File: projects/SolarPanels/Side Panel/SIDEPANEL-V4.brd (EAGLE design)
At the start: 99.5 x 82.5 mm, 27 parts

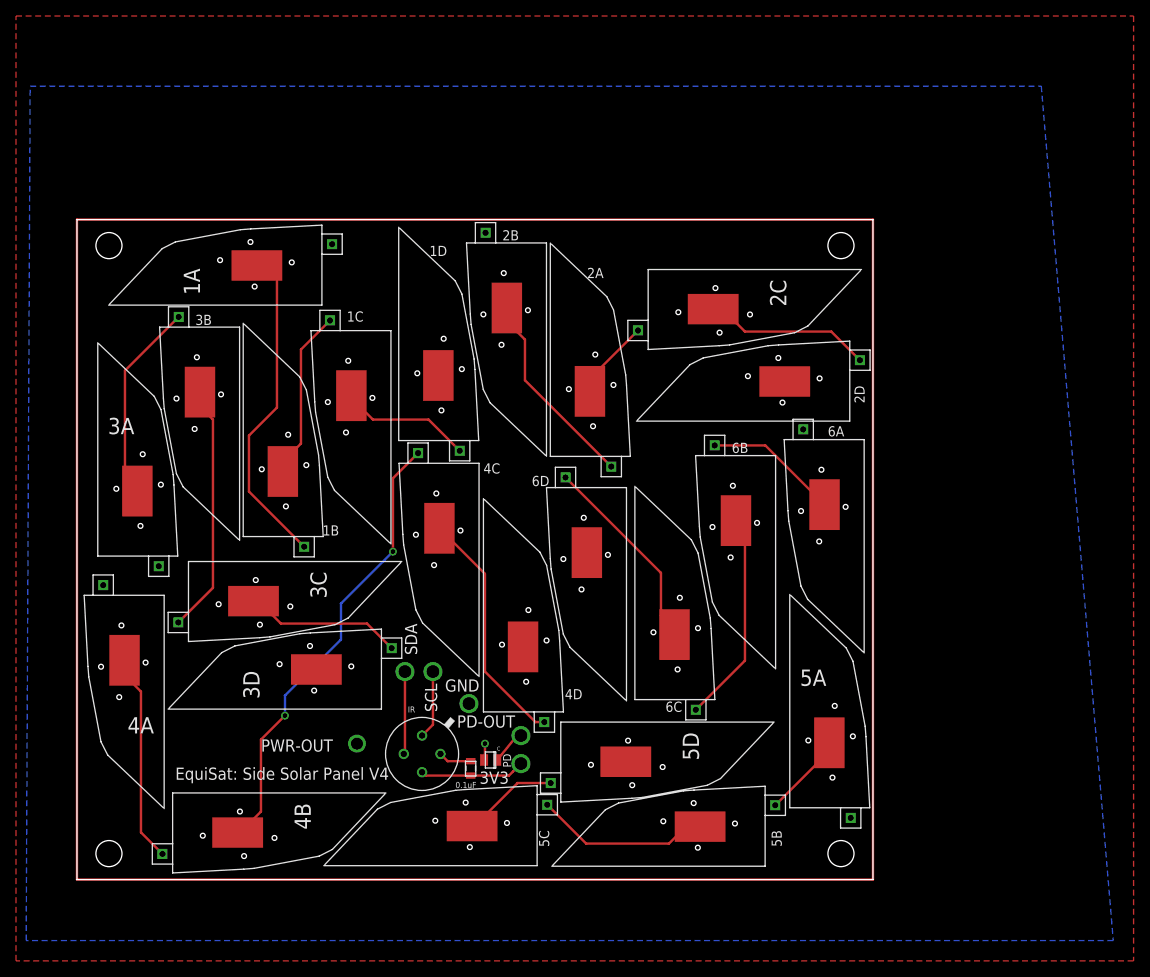
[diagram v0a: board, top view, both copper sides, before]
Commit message: Added top panel v4
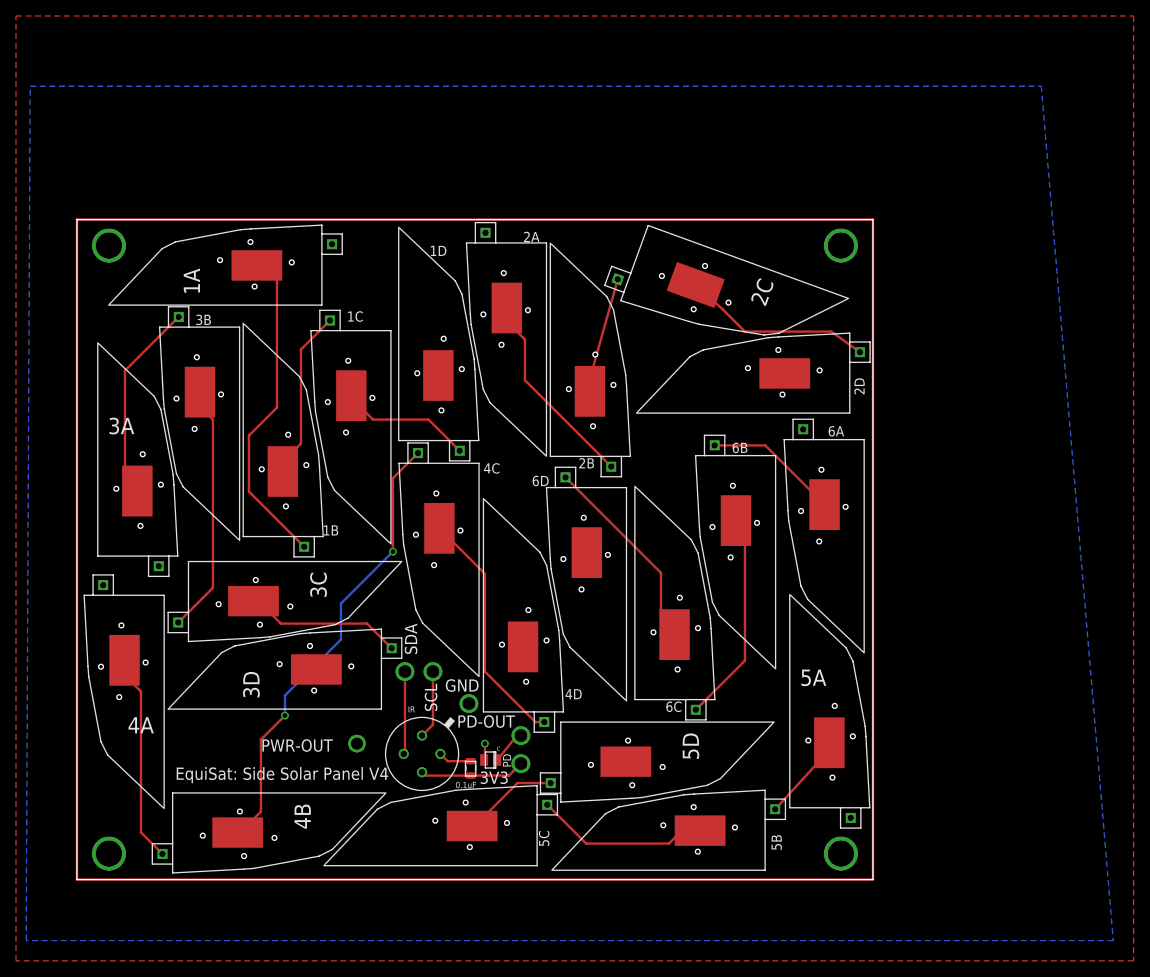
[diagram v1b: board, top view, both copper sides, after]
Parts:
- moved 2C 5.50 mm to (71.4, 81.8), turned to 250 degrees
- moved 2D 1.00 mm to (96.6, 58.3)
- moved 5B 0.50 mm to (86.0, 1.17)
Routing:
- net 2C: track 10.1 -> 14.5 mm
- net N$2: track 21.0 -> 23.7 mm
- net GND: vias 2 -> 6
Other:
- board text added: "September 2016"
- board text removed: "August 2016"
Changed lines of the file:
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@@
 <setting verticaltext="up"/>
 </settings>
-<grid distance="19.6850394" unitdist="mil" unit="mil" style="lines" multiple="1" display="no" altdistance="1.96850394" altunitdist="mil" altunit="mil"/>
+<grid distance="0.5" unitdist="mm" unit="mm" style="lines" multiple="1" display="no" altdistance="0.05" altunitdist="mm" altunit="mm"/>
 <layers>
 <layer number="1" name="Top" color="4" fill="1" visible="yes" active="yes"/>
@@
 <wire x1="99.5" y1="82.5" x2="0" y2="82.5" width="0" layer="20"/>
 <wire x1="0" y1="82.5" x2="0" y2="0" width="0" layer="20"/>
-<hole x="4" y="3.25" drill="3.26"/>
-<hole x="4" y="79.25" drill="3.26"/>
-<hole x="95.5" y="3.25" drill="3.26"/>
-<hole x="95.5" y="79.25" drill="3.26"/>
 <text x="32.5" y="16.5" size="1.524" layer="22" rot="MR0">PWR-OUT</text>
 <text x="40.5" y="24.5" size="1.524" layer="22" rot="MR270">SDA</text>
@@
 <text x="50.5" y="24" size="1.524" layer="22" rot="MR0">GND</text>
 <text x="38" y="50.5" size="1.524" layer="22" rot="MR270">EquiSat: Side Solar Panel V4</text>
-<text x="35.5" y="42" size="1.524" layer="22" rot="MR270">August 2016</text>
+<text x="35.5" y="42" size="1.524" layer="22" rot="MR270">September 2016</text>
 <text x="39" y="14" size="1.524" layer="21" rot="R180">EquiSat: Side Solar Panel V4</text>
 <text x="23" y="16" size="1.524" layer="21">PWR-OUT</text>
@@
 <polygon width="0.4064" layer="30">
 <vertex x="0" y="0"/>
-<vertex x="9" y="0"/>
-<vertex x="9" y="18"/>
-<vertex x="18" y="18"/>
-<vertex x="18" y="24"/>
-<vertex x="9" y="24"/>
-<vertex x="9" y="83.5"/>
+<vertex x="6.5" y="0"/>
+<vertex x="6.5" y="83.5"/>
 <vertex x="-5" y="83.5"/>
 <vertex x="-5" y="0"/>
@@
 </polygon>
 <polygon width="0.4064" layer="30">
-<vertex x="99.5" y="0"/>
-<vertex x="90.5" y="0"/>
-<vertex x="90.5" y="17.5"/>
-<vertex x="81" y="17.5"/>
-<vertex x="81" y="23.5"/>
-<vertex x="90.5" y="23.5"/>
-<vertex x="90.5" y="84.5"/>
+<vertex x="106.5" y="0"/>
+<vertex x="92" y="0"/>
+<vertex x="92" y="17.5"/>
+<vertex x="92.5" y="17.5"/>
+<vertex x="92.5" y="84.5"/>
 <vertex x="106.5" y="84.5"/>
-<vertex x="106.5" y="0"/>
 </polygon>
 </plain>
@@
 </element>
 <element name="1A" library="Solar Panel Parts" package="SOLARCELL2" value="NEWSOLARPANEL" x="30.62" y="71.81" rot="R90"/>
-<element name="2D" library="Solar Panel Parts" package="SOLARCELL2" value="NEWSOLARPANEL" x="96.6" y="57.31" smashed="yes" rot="R90">
-<attribute name="NAME" x="81.36" y="58.58" size="2.032" layer="25" rot="R90"/>
-<attribute name="NAME" x="97.19" y="61.75" size="1.27" layer="21" rot="R270"/>
-</element>
-<element name="2C" library="Solar Panel Parts" package="SOLARCELL2" value="NEWSOLARPANEL" x="71.4" y="76.26" rot="R270"/>
+<element name="2D" library="Solar Panel Parts" package="SOLARCELL2" value="NEWSOLARPANEL" x="96.6" y="58.31" smashed="yes" rot="R90">
+<attribute name="NAME" x="81.36" y="59.58" size="2.032" layer="25" rot="R90"/>
+<attribute name="NAME" x="97.19" y="62.75" size="1.27" layer="21" rot="R270"/>
+</element>
+<element name="2C" library="Solar Panel Parts" package="SOLARCELL2" value="NEWSOLARPANEL" x="71.4" y="81.76" rot="R250"/>
 <element name="2B" library="Solar Panel Parts" package="SOLARCELL2" value="NEWSOLARPANEL" x="59.17" y="52.9" smashed="yes">
 <attribute name="NAME" x="60.44" y="68.14" size="2.032" layer="25"/>
-<attribute name="NAME" x="55.25" y="81.17" size="1.27" layer="21" rot="R180"/>
+<attribute name="NAME" x="64.75" y="52.67" size="1.27" layer="21" rot="R180"/>
 </element>
 <element name="2A" library="Solar Panel Parts" package="SOLARCELL2" value="NEWSOLARPANEL" x="58.69" y="79.58" smashed="yes" rot="R180">
 <attribute name="NAME" x="57.42" y="64.34" size="2.032" layer="25" rot="R180"/>
-<attribute name="NAME" x="63.77" y="75.19" size="1.27" layer="21"/>
+<attribute name="NAME" x="55.77" y="79.69" size="1.27" layer="21"/>
 </element>
 <element name="3D" library="Solar Panel Parts" package="SOLARCELL2" value="NEWSOLARPANEL" x="38.06" y="21.31" rot="R90"/>
@@
 <attribute name="NAME" x="57.76" y="6.17" size="1.27" layer="21" rot="R270"/>
 </element>
-<element name="5B" library="Solar Panel Parts" package="SOLARCELL2" value="NEWSOLARPANEL" x="86.02" y="1.67" smashed="yes" rot="R90">
-<attribute name="NAME" x="70.78" y="2.94" size="2.032" layer="25" rot="R90"/>
-<attribute name="NAME" x="86.83" y="6.17" size="1.27" layer="21" rot="R270"/>
+<element name="5B" library="Solar Panel Parts" package="SOLARCELL2" value="NEWSOLARPANEL" x="86.02" y="1.17" smashed="yes" rot="R90">
+<attribute name="NAME" x="70.78" y="2.44" size="2.032" layer="25" rot="R90"/>
+<attribute name="NAME" x="86.83" y="5.67" size="1.27" layer="21" rot="R270"/>
 </element>
 <element name="5A" library="Solar Panel Parts" package="SOLARCELL2" value="NEWSOLARPANEL" x="89.1" y="8.98"/>
@@
 <wire x1="51" y1="15.06" x2="51" y2="17" width="0.3048" layer="1"/>
 <via x="49" y="22" extent="1-16" drill="1.6" shape="square"/>
+<via x="4" y="79.25" extent="1-16" drill="3.26"/>
+<via x="4" y="3.25" extent="1-16" drill="3.26"/>
+<via x="95.5" y="3.25" extent="1-16" drill="3.26"/>
+<via x="95.5" y="79.25" extent="1-16" drill="3.26"/>
 </signal>
 <signal name="SDA">
@@
 <contactref element="2D" pad="A"/>
 <contactref element="2C" pad="C"/>
-<wire x1="79.528" y1="71.307" x2="80.693" y2="71.307" width="0.3048" layer="1"/>
+<wire x1="77.34379375" y1="74.3257625" x2="80.693" y2="71.307" width="0.3048" layer="1"/>
 <wire x1="80.693" y1="71.307" x2="83.5" y2="68.5" width="0.3048" layer="1"/>
 <wire x1="83.5" y1="68.5" x2="94.3" y2="68.5" width="0.3048" layer="1"/>
-<wire x1="94.3" y1="68.5" x2="97.87" y2="64.93" width="0.3048" layer="1"/>
+<wire x1="94.3" y1="68.5" x2="97.87" y2="65.93" width="0.3048" layer="1"/>
 </signal>
 <signal name="N$3">
@@
 <contactref element="5C" pad="A"/>
 <contactref element="5B" pad="C"/>
-<wire x1="77.892" y1="6.623" x2="76.123" y2="6.623" width="0.3048" layer="1"/>
+<wire x1="77.892" y1="6.123" x2="76.123" y2="6.623" width="0.3048" layer="1"/>
 <wire x1="76.123" y1="6.623" x2="74" y2="4.5" width="0.3048" layer="1"/>
 <wire x1="74" y1="4.5" x2="63.65" y2="4.5" width="0.3048" layer="1"/>
@@
 <wire x1="94.053" y1="17.108" x2="92.553" y2="17.053" width="0.3048" layer="1"/>
 <wire x1="92.553" y1="17.053" x2="92.553" y2="14.553" width="0.3048" layer="1"/>
-<wire x1="92.553" y1="14.553" x2="87.29" y2="9.29" width="0.3048" layer="1"/>
+<wire x1="92.553" y1="14.553" x2="87.29" y2="8.79" width="0.3048" layer="1"/>
 </signal>
 <signal name="N$11">
@@
 <contactref element="2B" pad="C"/>
 <wire x1="64.123" y1="61.028" x2="64.123" y2="62.633" width="0.3048" layer="1"/>
-<wire x1="64.123" y1="62.633" x2="70.13" y2="68.64" width="0.3048" layer="1"/>
+<wire x1="64.123" y1="62.633" x2="67.600396875" y2="75.03390625" width="0.3048" layer="1"/>
 </signal>
 <signal name="N$15">

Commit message: Updated with processor test board V2
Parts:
- IR: device CNTRL_BOARD:MXL90614 -> CNTRL_BOARD:MXL90620
- moved 3A 1.50 mm to (1.10, 40.4)
- moved 3D 1.12 mm to (38.6, 20.3)
- moved 2B 0.71 mm to (59.7, 52.4)
- moved 3B 0.71 mm to (19.8, 68.6)
- moved 2C 0.50 mm to (71.4, 81.3), turned to 255 degrees
- moved 3C 0.50 mm to (13.4, 39.8)
- moved 4A 0.50 mm to (10.4, 35.5)
- moved 4B 0.50 mm to (12.0, 11.3)
- moved 4C 0.50 mm to (49.8, 52.0)
- moved 6B 0.50 mm to (87.8, 53.0)
- moved 6D 0.50 mm to (69.2, 49.0)
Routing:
- net N$3: track 19.7 -> 21.3 mm
- net SDA: track 10.4 -> 8.85 mm
- net N$18: track 25.2 -> 26.5 mm
- net N$17: track 25.2 -> 25.9 mm
- net N$12: track 56.9 -> 56.4 mm
- net 2C: track 14.5 -> 15.0 mm
- net N$8: track 16.8 -> 16.3 mm
